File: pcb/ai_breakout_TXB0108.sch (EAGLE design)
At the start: 8 parts, among them J1 1X10, J2 1X10

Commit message: small update schematic
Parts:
- IC1: value (none) -> TXB0108
- J2: value 1X10 -> 1X10NOFIRST; device Ai_Connectors:1X10 -> Ai_Connectors:1X10NOFIRST
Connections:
- net A1: now also J2.2; no longer J1.9
- net A2: now also J2.3; no longer J1.8
- net A3: now also J2.4; no longer J1.7
- net A4: now also J2.5; no longer J1.6
- net A5: now also J2.6; no longer J1.5
- net A6: now also J2.7; no longer J1.4
- net A7: now also J2.8; no longer J1.3
- net A8: now also J2.9; no longer J1.2
- net B1: now also J1.9; no longer J2.2
- net B2: now also J1.8; no longer J2.3
- net B3: now also J1.7; no longer J2.4
- net B4: now also J1.6; no longer J2.5
- net B5: now also J1.5; no longer J2.6
- net B6: now also J1.4; no longer J2.7
- net B7: now also J1.3; no longer J2.8
- net B8: now also J1.2; no longer J2.9
- net GND: now also J1.1; no longer J2.10
- net OE: now also J2.10; no longer J1.1
- net VCC-A: now also J2.1; no longer J1.10
- net VCC-B: now also J1.10; no longer J2.1
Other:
- moved on the sheet: J1, J2

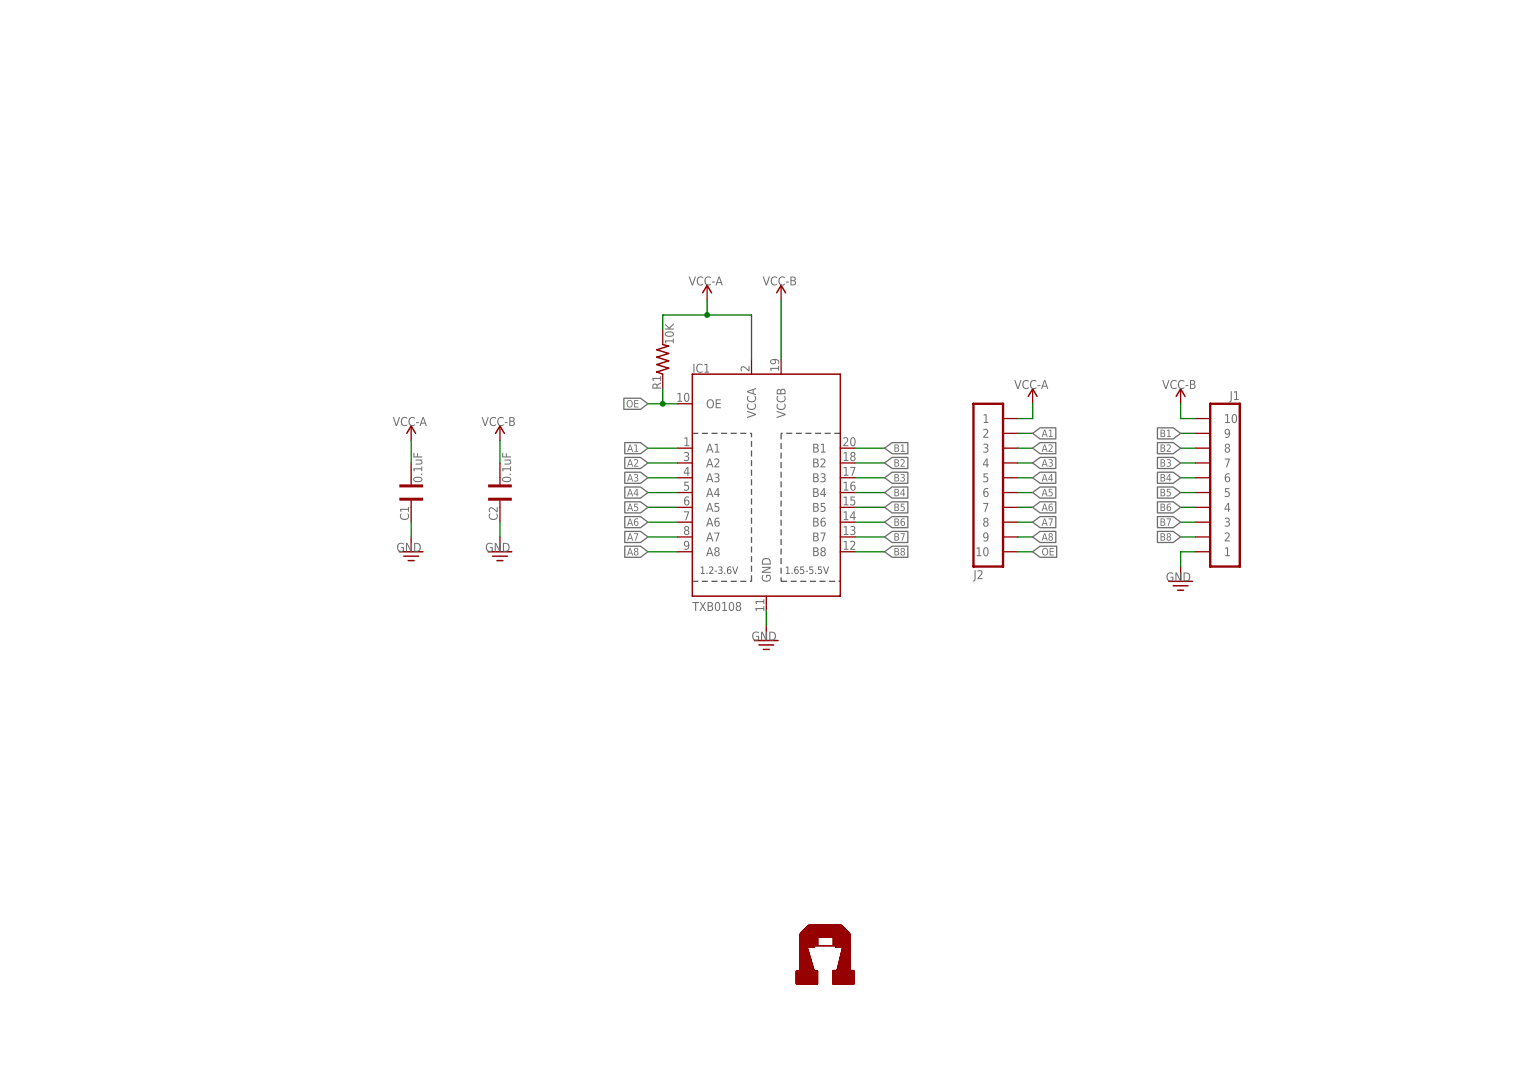
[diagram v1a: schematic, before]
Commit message: adding additional licensing information
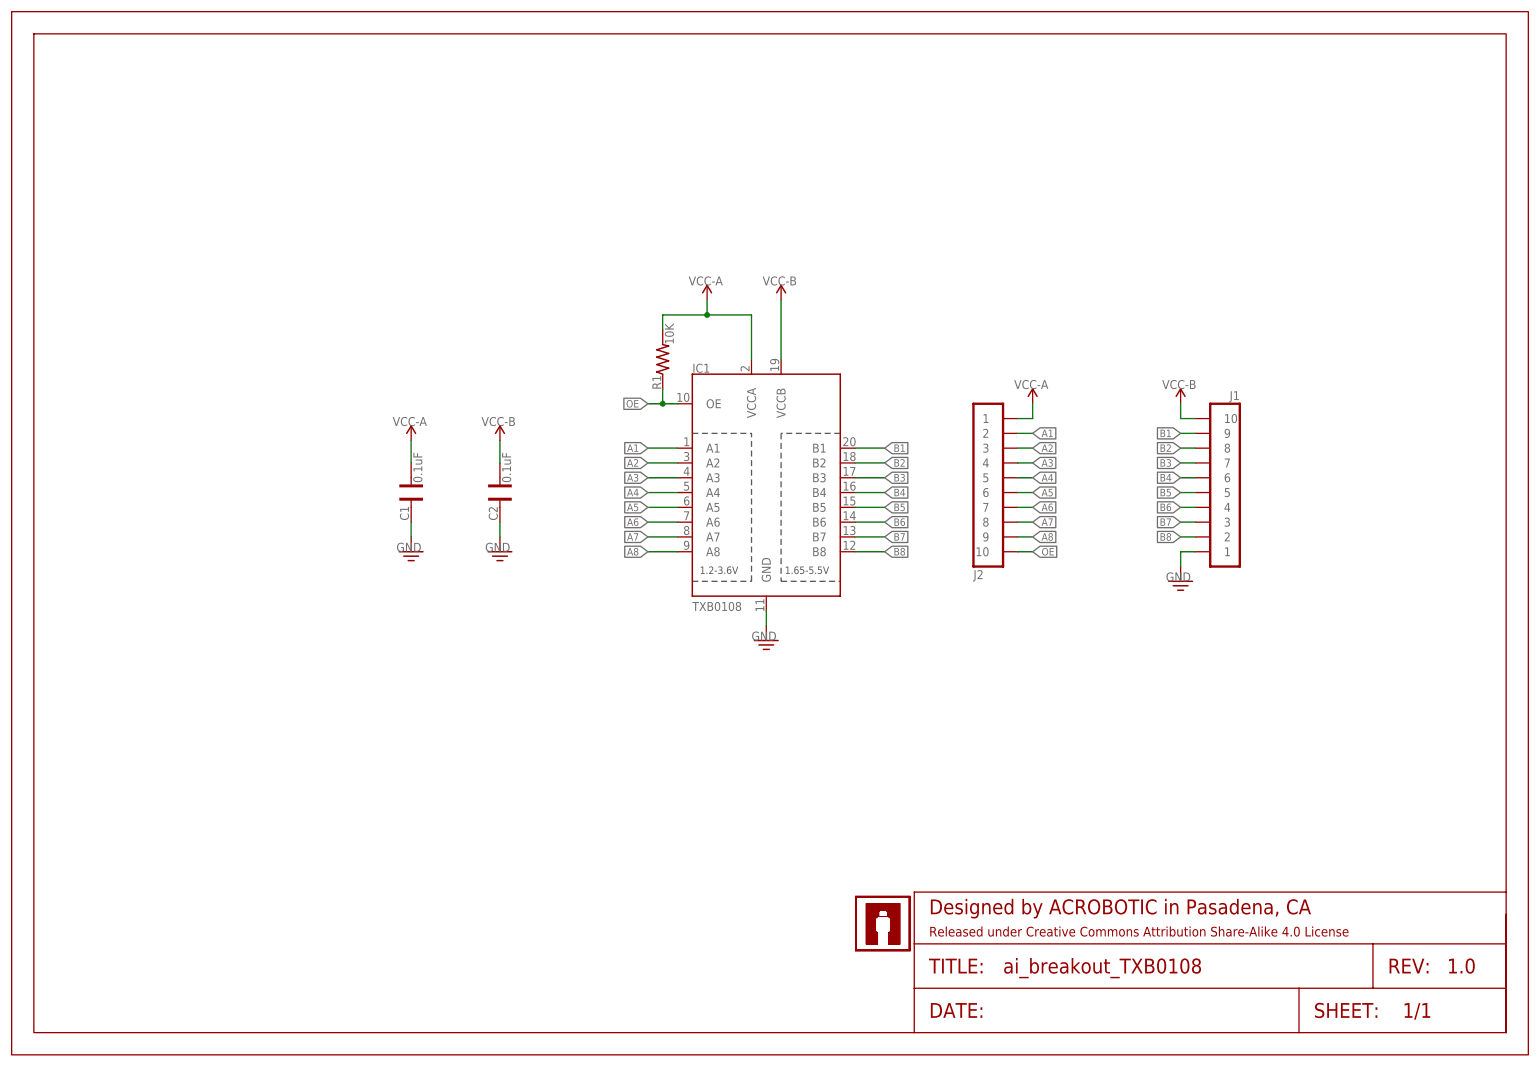
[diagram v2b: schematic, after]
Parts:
- added FRAME1: FRAME-LETTER, Ai_Miscellany:FRAME-LETTER
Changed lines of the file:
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@@
 <layer number="56" name="wert" color="7" fill="1" visible="no" active="no"/>
 <layer number="57" name="tCAD" color="7" fill="1" visible="no" active="no"/>
+<layer number="59" name="tCarbon" color="7" fill="1" visible="no" active="no"/>
+<layer number="60" name="bCarbon" color="7" fill="1" visible="no" active="no"/>
+<layer number="90" name="Modules" color="5" fill="1" visible="yes" active="yes"/>
 <layer number="91" name="Nets" color="2" fill="1" visible="yes" active="yes"/>
 <layer number="92" name="Busses" color="1" fill="1" visible="yes" active="yes"/>
@@
 <layer number="223" name="223bmp" color="24" fill="1" visible="no" active="no"/>
 <layer number="224" name="224bmp" color="25" fill="1" visible="no" active="no"/>
+<layer number="225" name="225bmp" color="7" fill="1" visible="yes" active="yes"/>
+<layer number="226" name="226bmp" color="7" fill="1" visible="yes" active="yes"/>
+<layer number="227" name="227bmp" color="7" fill="1" visible="yes" active="yes"/>
+<layer number="228" name="228bmp" color="7" fill="1" visible="yes" active="yes"/>
+<layer number="229" name="229bmp" color="7" fill="1" visible="yes" active="yes"/>
+<layer number="230" name="230bmp" color="7" fill="1" visible="yes" active="yes"/>
+<layer number="231" name="231bmp" color="7" fill="1" visible="yes" active="yes"/>
 <layer number="248" name="Housing" color="7" fill="1" visible="yes" active="yes"/>
 <layer number="249" name="Edge" color="7" fill="1" visible="yes" active="yes"/>
@@
 <layer number="251" name="SMDround" color="7" fill="1" visible="yes" active="yes"/>
 <layer number="254" name="cooling" color="7" fill="1" visible="yes" active="yes"/>
+<layer number="255" name="routoute" color="7" fill="1" visible="yes" active="yes"/>
 </layers>
 <schematic xreflabel="%F%N/%S.%C%R" xrefpart="/%S.%C%R">
@@
 <part name="R1" library="Ai_Passives" deviceset="RES" device="0603" value="10K"/>
 <part name="FRAME1" library="Ai_Miscellany" deviceset="FRAME-LETTER" device="">
-<attribute name="AUTHOR" value="A.I. HARDWARE SITH LORDS"/>
 <attribute name="REV" value="1.0"/>
 </part>
@@
 <instance part="R1" gate="G$1" x="111.76" y="119.38" rot="R90"/>
 <instance part="FRAME1" gate="G$1" x="0" y="0"/>
-<instance part="FRAME1" gate="G$2" x="147.32" y="0"/>
-<instance part="U$1" gate="G$1" x="139.7" y="16.51"/>
-<instance part="U$2" gate="G$1" x="139.7" y="16.51"/>
+<instance part="FRAME1" gate="G$2" x="154.94" y="3.81"/>
+<instance part="U$1" gate="G$1" x="144.78" y="17.78"/>
+<instance part="U$2" gate="G$1" x="144.78" y="17.78"/>
 <instance part="U$3" gate="G$1" x="68.58" y="105.41"/>
 <instance part="U$4" gate="G$1" x="119.38" y="129.54"/>
@@
 </schematic>
 </drawing>
+<compatibility>
+<note version="6.3" minversion="6.2.2" severity="warning">
+Since Version 6.2.2 text objects can contain more than one line,
+which will not be processed correctly with this version.
+</note>
+</compatibility>
 </eagle>
